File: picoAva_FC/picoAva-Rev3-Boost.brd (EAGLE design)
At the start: 55.5 x 24.8 mm, 26 parts, among them IC2 TPS61201, J1 AVR_SPI_PRG_6PTH, U1 ATMEGA328

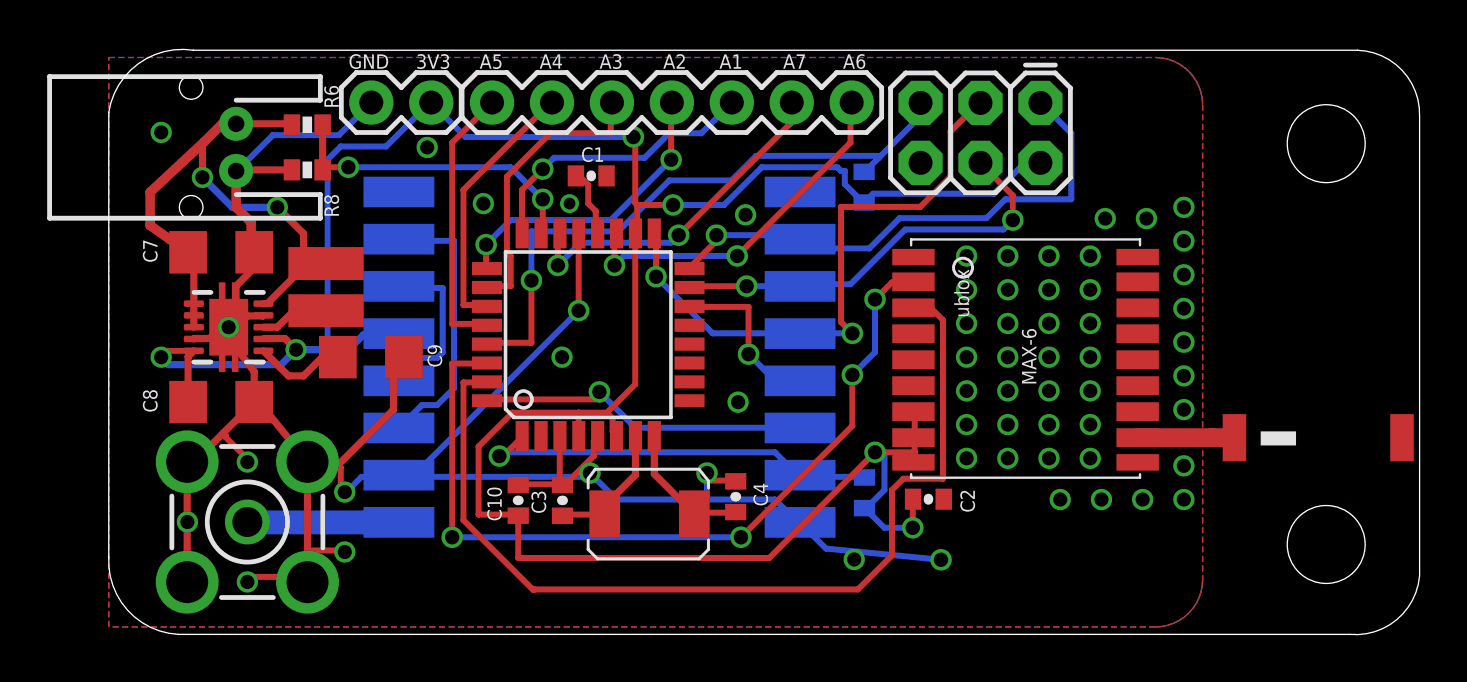
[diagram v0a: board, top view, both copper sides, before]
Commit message: Removed older versions
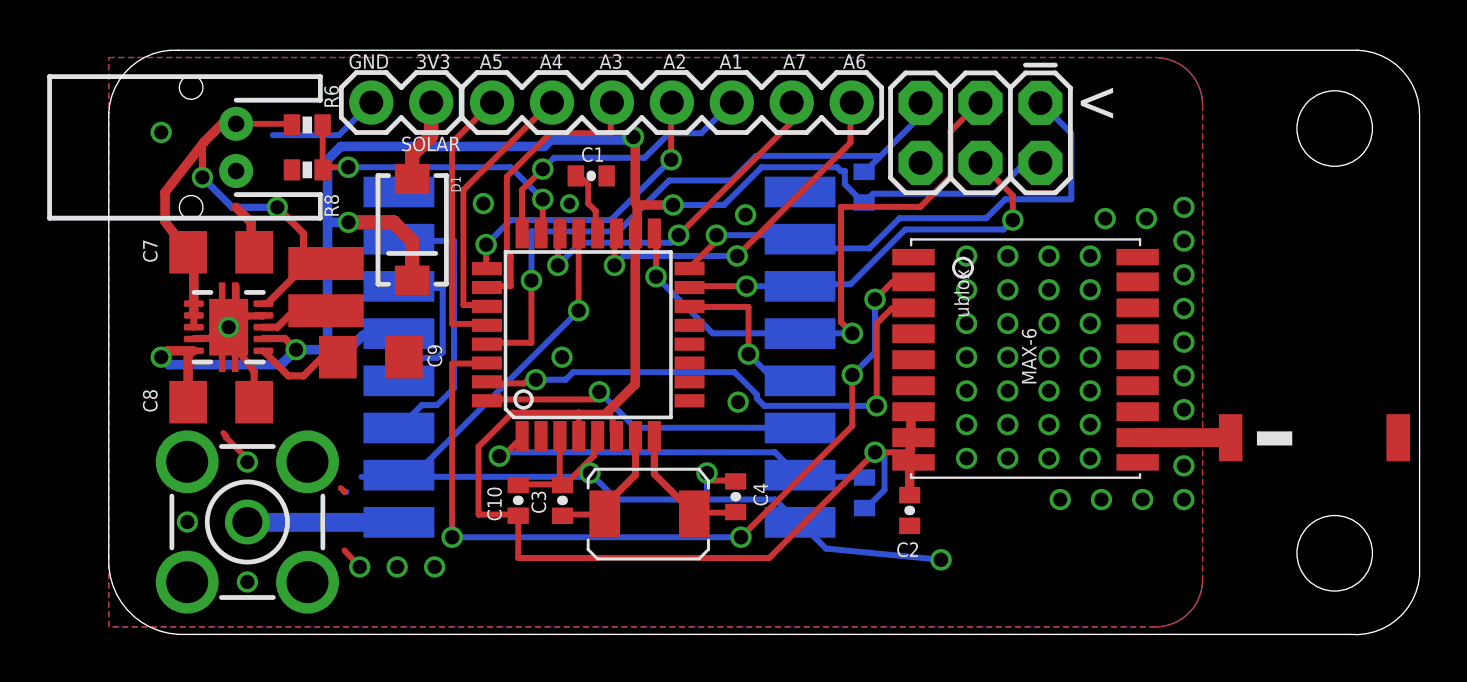
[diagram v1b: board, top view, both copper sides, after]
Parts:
- removed JP1, JP2: STAND-OFF, SparkFun:STAND-OFF
- added D1: (no value), SparkFun:SMA-DIODE
- moved C2 0.93 mm to (33.0, 60.8), turned to 270 degrees
- moved U$3 0.16 mm to (50.4, 65.2)
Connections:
- new net N$1: D1.A, JP3.1
- net VCC: now also D1.C; no longer JP3.1
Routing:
- net GND: track 106.1 -> 70.0 mm, vias 60 -> 59
- net UBLOX_RXD: track 40.1 -> 22.8 mm, vias 0 -> 2
- net N$1: track 0.00 -> 3.58 mm
- net VCC: track 112.6 -> 115.4 mm
- net VBATT: track 25.8 -> 24.8 mm
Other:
- outline, holes or cut-outs redrawn
- board text added: "<"
- board text added: "If found contact ukhasrecovery@gmail.com"
- board text added: "SOLAR"
- board text added: "µAva2-B"
- board text removed: "µAva-RB"
